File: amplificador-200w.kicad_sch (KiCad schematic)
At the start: 34 parts, among them J1 IN, J10 MH, J11 MH, J12 FAN, J2 AUX, J3 PWR, J4 out, J5 out, J6 out, J7 out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

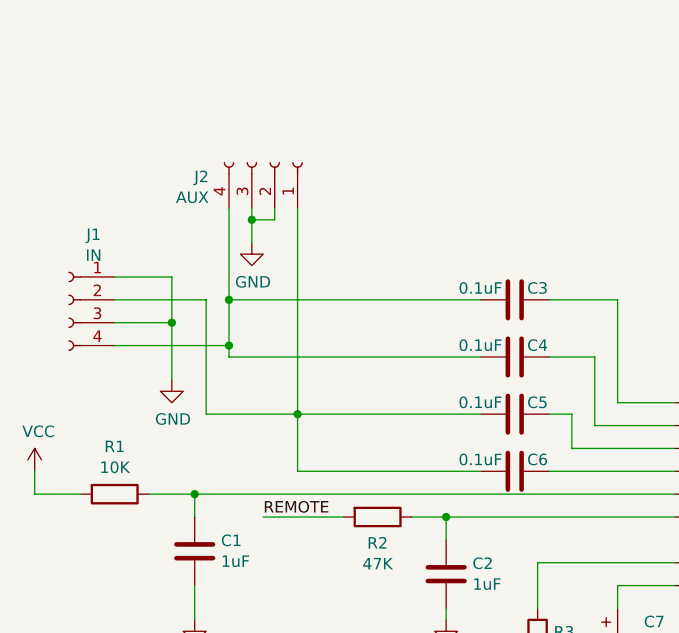
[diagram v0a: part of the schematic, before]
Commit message: quitando la entrada de audio auxiliar
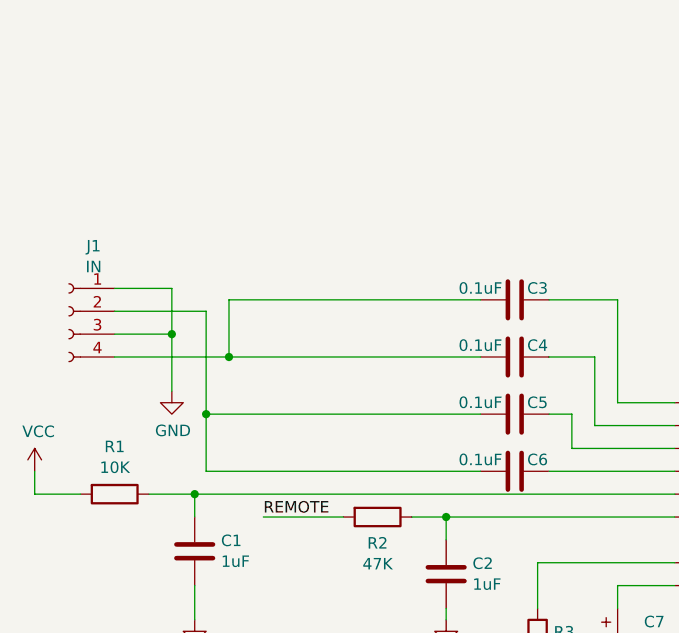
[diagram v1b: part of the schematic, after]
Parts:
- removed J2: AUX, Connector_PinHeader_2.54mm:PinHeader_1x04_P2.54mm_Vertical, symbol amplificador-200w-rescue:Conn_01x04_Female-Connector
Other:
- moved on the sheet: J1
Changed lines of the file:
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@@
     (company "MaykolRey.com")
   )
-  (junction (at 74.93 85.09) (diameter 0) (color 0 0 0 0)
-  )
   (junction (at 179.07 127) (diameter 0) (color 0 0 0 0)
   )
   (junction (at 179.07 129.54) (diameter 0) (color 0 0 0 0)
   )
-  (junction (at 82.55 97.79) (diameter 0) (color 0 0 0 0)
-  )
   (junction (at 209.55 66.04) (diameter 0) (color 0 0 0 0)
   )
-  (junction (at 77.47 76.2) (diameter 0) (color 0 0 0 0)
-  )
   (junction (at 177.8 66.04) (diameter 0) (color 0 0 0 0)
   )
@@
   (junction (at 222.25 43.18) (diameter 0) (color 0 0 0 0)
   )
+  (junction (at 74.93 91.44) (diameter 0) (color 0 0 0 0)
+  )
   (junction (at 66.04 167.64) (diameter 0) (color 0 0 0 0)
   )
@@
   (junction (at 177.8 43.18) (diameter 0) (color 0 0 0 0)
   )
-  (junction (at 74.93 90.17) (diameter 0) (color 0 0 0 0)
-  )
   (junction (at 73.66 167.64) (diameter 0) (color 0 0 0 0)
   )
@@
   (junction (at 177.8 88.9) (diameter 0) (color 0 0 0 0)
   )
+  (junction (at 72.39 97.79) (diameter 0) (color 0 0 0 0)
+  )
   (junction (at 71.12 106.68) (diameter 0) (color 0 0 0 0)
   )
   (junction (at 196.85 43.18) (diameter 0) (color 0 0 0 0)
   )
-  (junction (at 68.58 87.63) (diameter 0) (color 0 0 0 0)
+  (junction (at 68.58 88.9) (diameter 0) (color 0 0 0 0)
   )
   (wire (pts (xy 177.8 66.04) (xy 184.15 66.04))
@@
     (stroke (width 0) (type default))
   )
-  (wire (pts (xy 62.23 90.17) (xy 74.93 90.17))
+  (wire (pts (xy 62.23 91.44) (xy 74.93 91.44))
     (stroke (width 0) (type default))
   )
@@
     (stroke (width 0) (type default))
   )
-  (wire (pts (xy 82.55 74.93) (xy 82.55 97.79))
-    (stroke (width 0) (type default))
-  )
   (wire (pts (xy 186.69 96.52) (xy 170.18 96.52))
     (stroke (width 0) (type default))
@@
     (stroke (width 0) (type default))
   )
-  (wire (pts (xy 80.01 76.2) (xy 77.47 76.2))
-    (stroke (width 0) (type default))
-  )
-  (wire (pts (xy 82.55 104.14) (xy 82.55 97.79))
+  (wire (pts (xy 72.39 104.14) (xy 72.39 97.79))
     (stroke (width 0) (type default))
   )
@@
     (stroke (width 0) (type default))
   )
-  (wire (pts (xy 68.58 82.55) (xy 68.58 87.63))
+  (wire (pts (xy 68.58 83.82) (xy 68.58 88.9))
     (stroke (width 0) (type default))
   )
@@
     (stroke (width 0) (type default))
   )
-  (wire (pts (xy 77.47 74.93) (xy 77.47 76.2))
-    (stroke (width 0) (type default))
-  )
   (wire (pts (xy 87.63 109.22) (xy 78.74 109.22))
     (stroke (width 0) (type default))
@@
     (stroke (width 0) (type default))
   )
-  (wire (pts (xy 82.55 97.79) (xy 102.87 97.79))
-    (stroke (width 0) (type default))
-  )
   (wire (pts (xy 222.25 77.47) (xy 222.25 74.93))
     (stroke (width 0) (type default))
@@
     (stroke (width 0) (type default))
   )
-  (wire (pts (xy 62.23 82.55) (xy 68.58 82.55))
+  (wire (pts (xy 62.23 83.82) (xy 68.58 83.82))
     (stroke (width 0) (type default))
   )
@@
     (stroke (width 0) (type default))
   )
-  (wire (pts (xy 80.01 74.93) (xy 80.01 76.2))
-    (stroke (width 0) (type default))
-  )
   (wire (pts (xy 158.75 68.58) (xy 158.75 69.85))
     (stroke (width 0) (type default))
@@
     (stroke (width 0) (type default))
   )
-  (wire (pts (xy 82.55 104.14) (xy 102.87 104.14))
+  (wire (pts (xy 72.39 104.14) (xy 102.87 104.14))
     (stroke (width 0) (type default))
   )
@@
     (stroke (width 0) (type default))
   )
-  (wire (pts (xy 72.39 85.09) (xy 72.39 97.79))
-    (stroke (width 0) (type default))
-  )
-  (wire (pts (xy 72.39 97.79) (xy 82.55 97.79))
-    (stroke (width 0) (type default))
-  )
-  (wire (pts (xy 62.23 87.63) (xy 68.58 87.63))
+  (wire (pts (xy 72.39 86.36) (xy 72.39 97.79))
+    (stroke (width 0) (type default))
+  )
+  (wire (pts (xy 72.39 97.79) (xy 102.87 97.79))
+    (stroke (width 0) (type default))
+  )
+  (wire (pts (xy 62.23 88.9) (xy 68.58 88.9))
     (stroke (width 0) (type default))
   )
@@
     (stroke (width 0) (type default))
   )
-  (wire (pts (xy 72.39 85.09) (xy 62.23 85.09))
+  (wire (pts (xy 72.39 86.36) (xy 62.23 86.36))
     (stroke (width 0) (type default))
   )
@@
     (stroke (width 0) (type default))
   )
+  (wire (pts (xy 74.93 85.09) (xy 74.93 91.44))
+    (stroke (width 0) (type default))
+  )
   (wire (pts (xy 158.75 68.58) (xy 151.13 68.58))
     (stroke (width 0) (type default))
@@
     (stroke (width 0) (type default))
   )
-  (wire (pts (xy 74.93 91.44) (xy 74.93 90.17))
-    (stroke (width 0) (type default))
-  )
-  (wire (pts (xy 68.58 87.63) (xy 68.58 93.98))
+  (wire (pts (xy 68.58 88.9) (xy 68.58 95.25))
     (stroke (width 0) (type default))
   )
@@
     (stroke (width 0) (type default))
   )
-  (wire (pts (xy 77.47 76.2) (xy 77.47 78.74))
-    (stroke (width 0) (type default))
-  )
   (wire (pts (xy 179.07 143.51) (xy 179.07 137.16))
     (stroke (width 0) (type default))
@@
     (stroke (width 0) (type default))
   )
-  (wire (pts (xy 74.93 90.17) (xy 74.93 85.09))
-    (stroke (width 0) (type default))
-  )
   (wire (pts (xy 158.75 63.5) (xy 151.13 63.5))
     (stroke (width 0) (type default))
@@
   )
   (wire (pts (xy 71.12 109.22) (xy 71.12 106.68))
-    (stroke (width 0) (type default))
-  )
-  (wire (pts (xy 74.93 74.93) (xy 74.93 85.09))
     (stroke (width 0) (type default))
   )
@@
     )
   )
-  (symbol (lib_id "amplificador-200w-rescue:Conn_01x04_Female-Connector") (at 57.15 85.09 0) (mirror y) (unit 1)
-    (in_bom yes) (on_board yes) (dnp no)
-    (property "Reference" "J1" (at 59.8932 77.851 0)
-      (effects (font (size 1.27 1.27)))
-    )
-    (property "Value" "IN" (at 59.8932 80.1624 0)
-      (effects (font (size 1.27 1.27)))
-    )
-    (property "Footprint" "MSS_Connector:CUI_RCJ-21XX" (at 57.15 85.09 0)
-      (effects (font (size 1.27 1.27)) hide)
-    )
-    (property "Datasheet" "~" (at 57.15 85.09 0)
-      (effects (font (size 1.27 1.27)) hide)
-    )
-    (property "Mfg Part #" "RCJ-2121" (at 57.15 85.09 0)
+  (symbol (lib_id "amplificador-200w-rescue:Conn_01x04_Female-Connector") (at 57.15 86.36 0) (mirror y) (unit 1)
+    (in_bom yes) (on_board yes) (dnp no)
+    (property "Reference" "J1" (at 59.8932 79.121 0)
+      (effects (font (size 1.27 1.27)))
+    )
+    (property "Value" "IN" (at 59.8932 81.4324 0)
+      (effects (font (size 1.27 1.27)))
+    )
+    (property "Footprint" "MSS_Connector:CUI_RCJ-21XX" (at 57.15 86.36 0)
+      (effects (font (size 1.27 1.27)) hide)
+    )
+    (property "Datasheet" "~" (at 57.15 86.36 0)
+      (effects (font (size 1.27 1.27)) hide)
+    )
+    (property "Mfg Part #" "RCJ-2121" (at 57.15 86.36 0)
       (effects (font (size 1.27 1.27)) hide)
     )
@@
     )
   )
-  (symbol (lib_id "amplificador-200w-rescue:Conn_01x04_Female-Connector") (at 80.01 69.85 270) (mirror x) (unit 1)
-    (in_bom yes) (on_board yes) (dnp no)
-    (property "Reference" "J2" (at 72.6948 71.4248 90)
-      (effects (font (size 1.27 1.27)) (justify right))
-    )
-    (property "Value" "AUX" (at 72.6948 73.7362 90)
-      (effects (font (size 1.27 1.27)) (justify right))
-    )
-    (property "Footprint" "Connector_PinHeader_2.54mm:PinHeader_1x04_P2.54mm_Vertical" (at 80.01 69.85 0)
-      (effects (font (size 1.27 1.27)) hide)
-    )
-    (property "Datasheet" "~" (at 80.01 69.85 0)
-      (effects (font (size 1.27 1.27)) hide)
-    )
-    (pin "1")
-    (pin "2")
-    (pin "3")
-    (pin "4")
-    (instances
-      (project "amplificador-200w"
-        (path "/39914e79-27c0-408c-80f2-4ede19bf9413"
-          (reference "J2") (unit 1)
-        )
-      )
-    )
-  )
   (symbol (lib_id "power:GND") (at 69.85 170.18 0) (unit 1)
     (in_bom yes) (on_board yes) (dnp no)
@@
     )
   )
-  (symbol (lib_id "power:GND") (at 77.47 78.74 0) (unit 1)
-    (in_bom yes) (on_board yes) (dnp no)
-    (property "Reference" "#PWR04" (at 77.47 85.09 0)
-      (effects (font (size 1.27 1.27)) hide)
-    )
-    (property "Value" "GND" (at 77.597 83.1342 0)
-      (effects (font (size 1.27 1.27)))
-    )
-    (property "Footprint" "" (at 77.47 78.74 0)
-      (effects (font (size 1.27 1.27)) hide)
-    )
-    (property "Datasheet" "" (at 77.47 78.74 0)
-      (effects (font (size 1.27 1.27)) hide)
-    )
-    (pin "1")
-    (instances
-      (project "amplificador-200w"
-        (path "/39914e79-27c0-408c-80f2-4ede19bf9413"
-          (reference "#PWR04") (unit 1)
-        )
-      )
-    )
-  )
   (symbol (lib_id "amplificador-200w-rescue:Conn_01x02_Male-Connector") (at 242.57 45.72 180) (unit 1)
     (in_bom yes) (on_board yes) (dnp no)
@@
     )
   )
-  (symbol (lib_id "power:GND") (at 68.58 93.98 0) (unit 1)
-    (in_bom yes) (on_board yes) (dnp no)
-    (property "Reference" "#PWR02" (at 68.58 100.33 0)
-      (effects (font (size 1.27 1.27)) hide)
-    )
-    (property "Value" "GND" (at 68.707 98.3742 0)
-      (effects (font (size 1.27 1.27)))
-    )
-    (property "Footprint" "" (at 68.58 93.98 0)
-      (effects (font (size 1.27 1.27)) hide)
-    )
-    (property "Datasheet" "" (at 68.58 93.98 0)
-      (effects (font (size 1.27 1.27)) hide)
-    )
+  (symbol (lib_id "power:GND") (at 68.58 95.25 0) (unit 1)
+    (in_bom yes) (on_board yes) (dnp no)
+    (property "Reference" "#PWR02" (at 68.58 101.6 0)
+      (effects (font (size 1.27 1.27)) hide)
+    )
+    (property "Value" "GND" (at 68.707 99.6442 0)
+      (effects (font (size 1.27 1.27)))
+    )
+    (property "Footprint" "" (at 68.58 95.25 0)
+      (effects (font (size 1.27 1.27)) hide)
+    )
+    (property "Datasheet" "" (at 68.58 95.25 0)
+      (effects (font (size 1.27 1.27)) hide)
+    )

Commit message: version 2 enviada a fabricar
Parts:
- added C18: 100nF, Capacitor_SMD:C_0603_1608Metric_Pad1.08x0.95mm_HandSolder, symbol Device:C
- added D2: D_ALT, Diode_SMD:D_SMA, symbol Device:D
- added D3: LED, LED_THT:LED_D3.0mm, symbol Device:LED
- added R4: 10K, Resistor_SMD:R_0603_1608Metric, symbol Device:R_US
- added RV1: R_Potentiometer_Dual, Potentiometer_THT:Potentiometer_Alps_RK097_Dual_Horizontal, symbol Device:R_Potentiometer_Dual
- C1, C2: footprint Capacitor_THT:C_Disc_D4.3mm_W1.9mm_P5.00mm -> Capacitor_SMD:C_0805_2012Metric
- C10, C11, C12, C14, C15, C16, C17, C7, C8: symbol amplificador-200w-rescue:CP1-Device -> Device:C_Polarized_US
- C13, C3, C4, C5, C6: value 0.1uF -> 100nF; footprint Capacitor_THT:C_Disc_D4.3mm_W1.9mm_P5.00mm -> Capacitor_SMD:C_0603_1608Metric_Pad1.08x0.95mm_HandSolder
- C9: footprint Capacitor_THT:C_Disc_D4.3mm_W1.9mm_P5.00mm -> Capacitor_SMD:C_0603_1608Metric_Pad1.08x0.95mm_HandSolder
- D1: footprint Diode_THT:D_DO-15_P12.70mm_Horizontal -> Diode_SMD:D_SMA; symbol amplificador-200w-rescue:D_ALT-Device -> Device:D
- J12: footprint Connector_PinHeader_2.54mm:PinHeader_1x02_P2.54mm_Vertical -> Connector_JST:JST_PH_B2B-PH-K_1x02_P2.00mm_Vertical
- R1, R2, R3: footprint Resistor_THT:R_Axial_DIN0411_L9.9mm_D3.6mm_P12.70mm_Horizontal -> Resistor_SMD:R_0603_1608Metric; symbol Device:R -> Device:R_US
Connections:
- net GND: now also C18.2, D3.1 (K)
- net REMOTE: now also D2.1 (K); no longer J3.1 (Pin_1)
- net IN_LEFT_P: now reaches C3.2, C4.2
- net IN_LEFT_P: now also RV1.4, RV1.5; no longer J1.4 (Pin_4)
- net IN_RIGTH_P: now reaches C5.2, C6.2
- net IN_RIGTH_P: now also RV1.1, RV1.2; no longer J1.2 (Pin_2)
- net VCC renamed +12V
- net +12V: now also C18.1, R4.1
- new net: D2.2 (A), J3.1 (Pin_1)
- new net: D3.2 (A), R4.2
- new net IN_LEFT: J1.4 (Pin_4), RV1.6
- new net IN_RIGTH: J1.2 (Pin_2), RV1.3
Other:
- moved on the sheet: C1, C10, C11, C12, C13, C14, C15, C16, C17, C2, C3, C4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

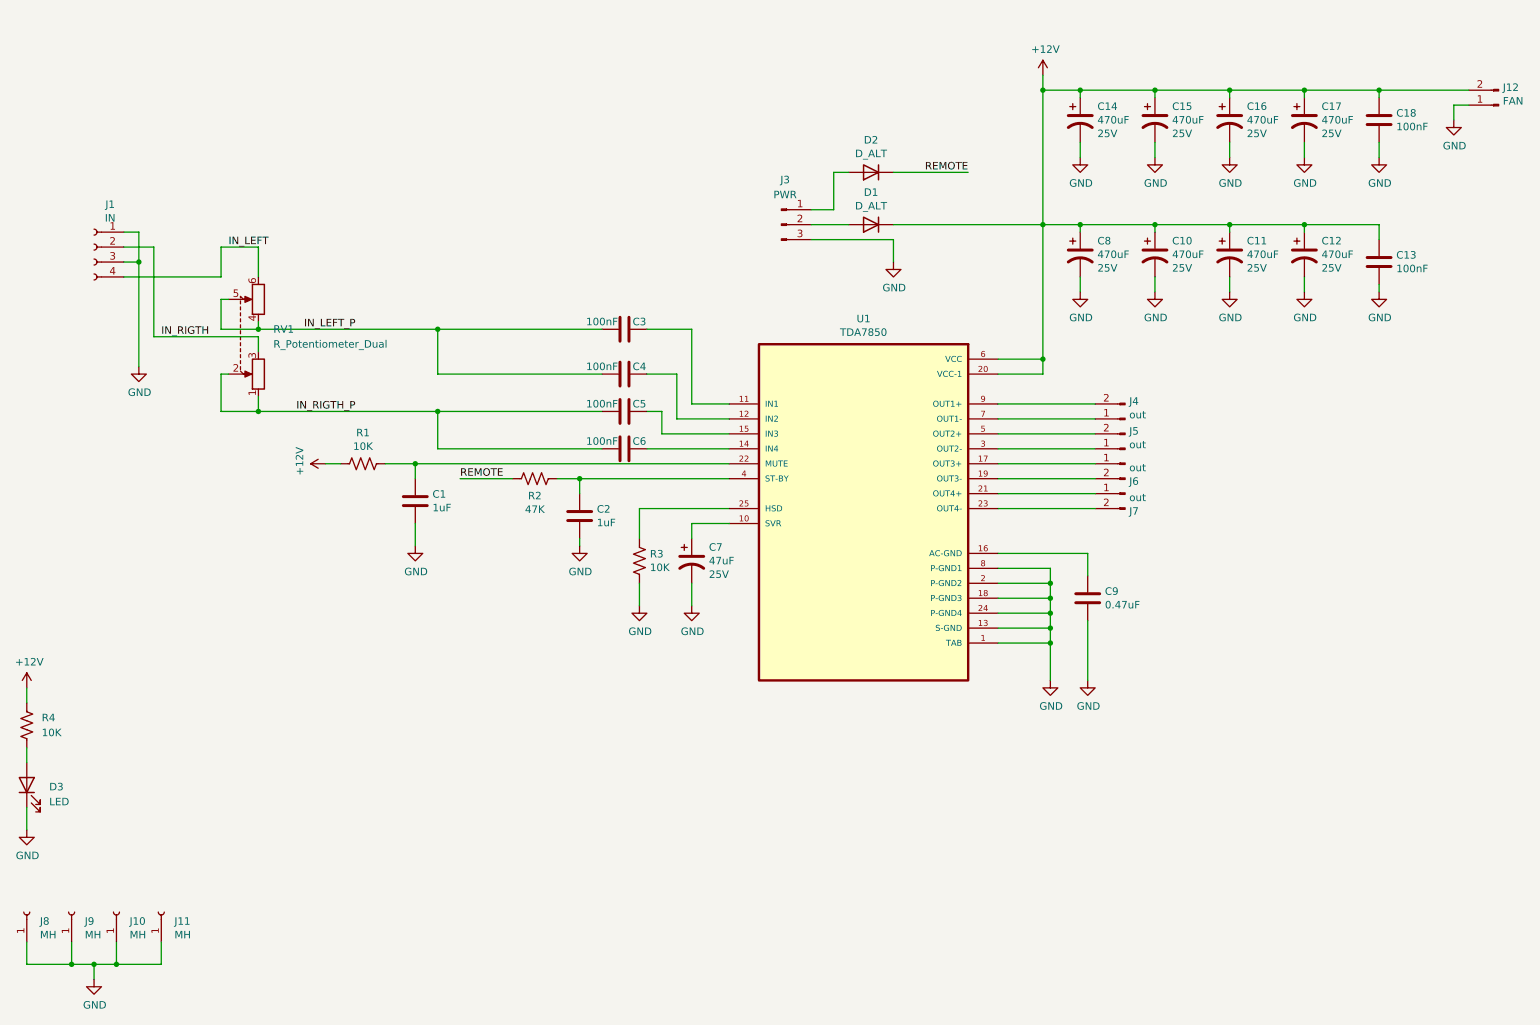
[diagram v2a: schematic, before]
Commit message: corrgiendo disipador y que el ventilador solo prenda con remote
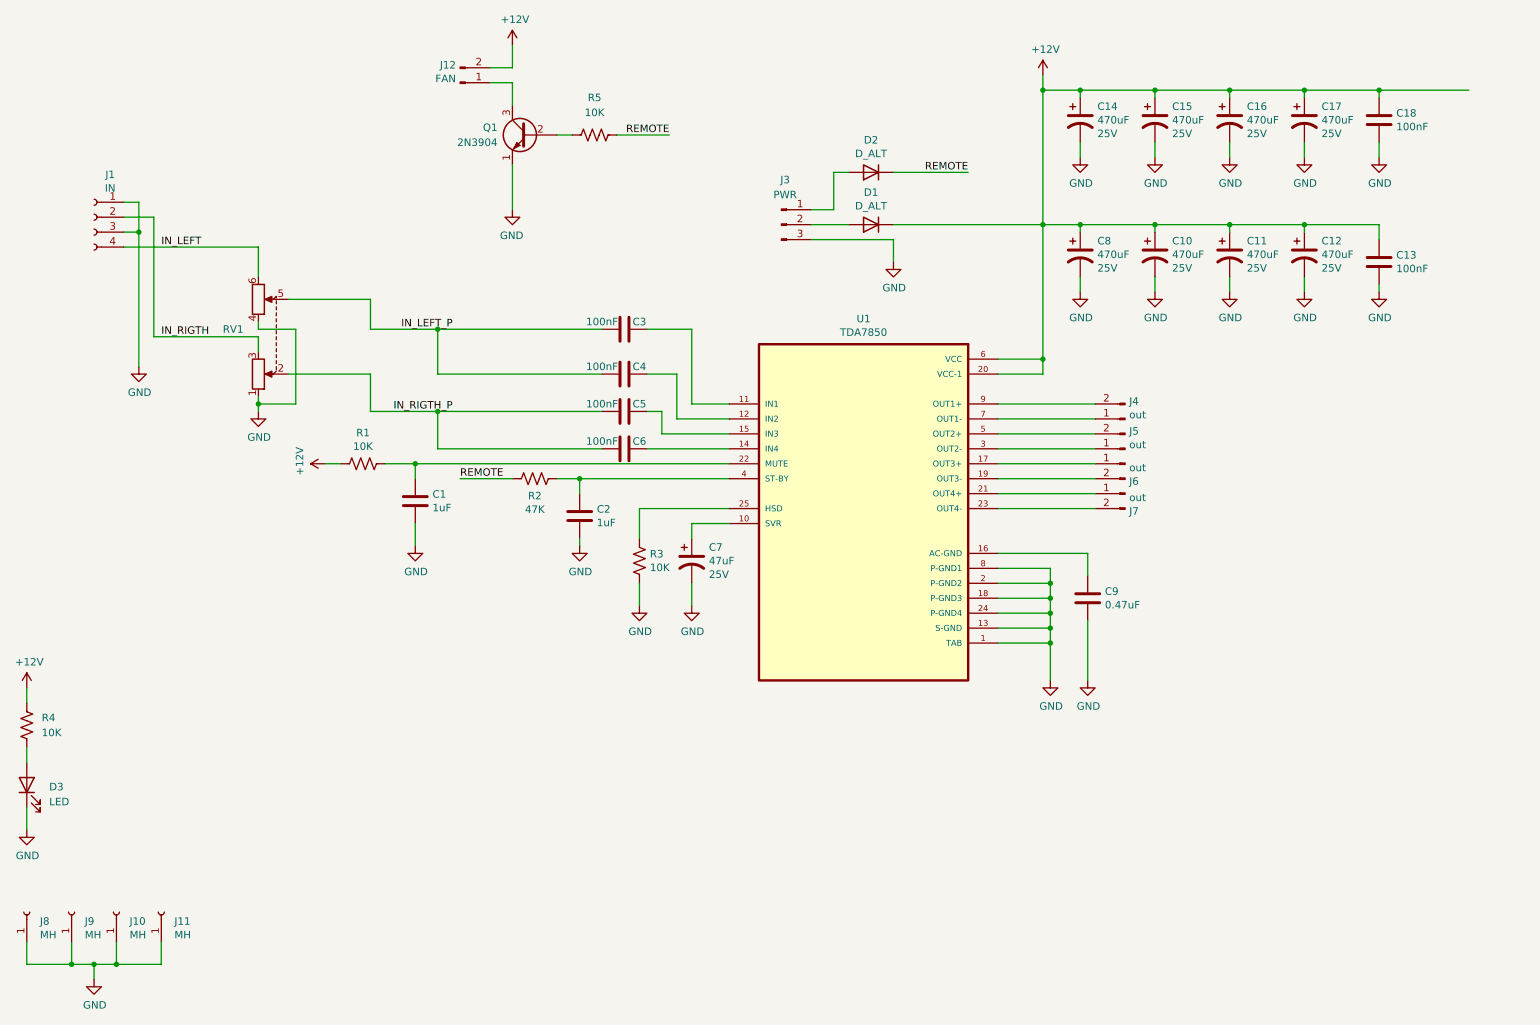
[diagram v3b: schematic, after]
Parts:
- added Q1: 2N3904, Package_TO_SOT_THT:TO-92_Inline, symbol Transistor_BJT:2N3904
- added R5: 10K, Resistor_SMD:R_0603_1608Metric, symbol Device:R_US
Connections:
- net GND: now also RV1.1, RV1.4, Q1.1 (E); no longer J12.1 (Pin_1)
- net IN_LEFT_P: no longer RV1.4
- net IN_RIGTH_P: no longer RV1.1
- net REMOTE: now also R5.2
- new net: J12.1 (Pin_1), Q1.3 (C)
- new net: Q1.2 (B), R5.1
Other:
- moved on the sheet: J1, J12, RV1
